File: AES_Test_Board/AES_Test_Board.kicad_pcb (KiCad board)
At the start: 2 copper layers, 60 x 65 mm, 36 parts, among them J1 Conn_02x06_Top_Bottom, J2 Conn_02x06_Top_Bottom, U3 TCR3RM10A

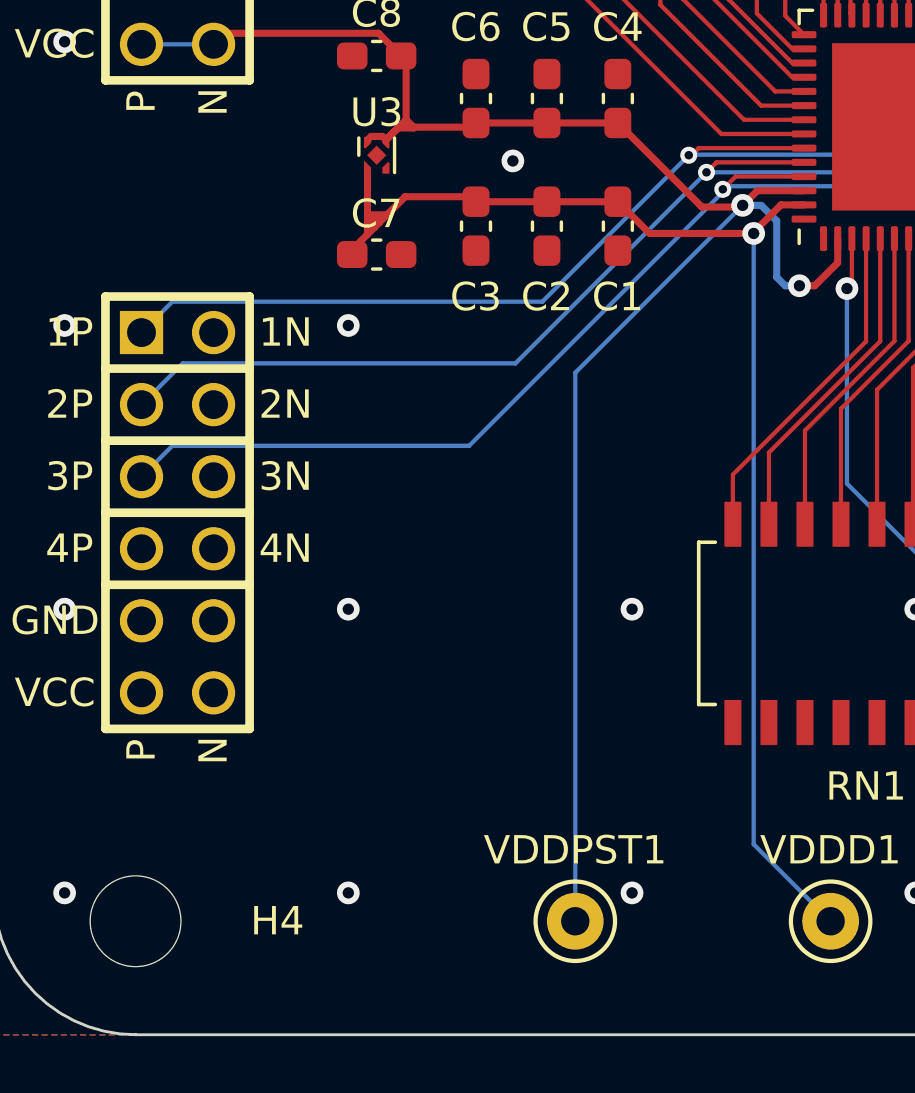
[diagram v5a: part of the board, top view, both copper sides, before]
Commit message: Created Bitstreams for both FPGA's
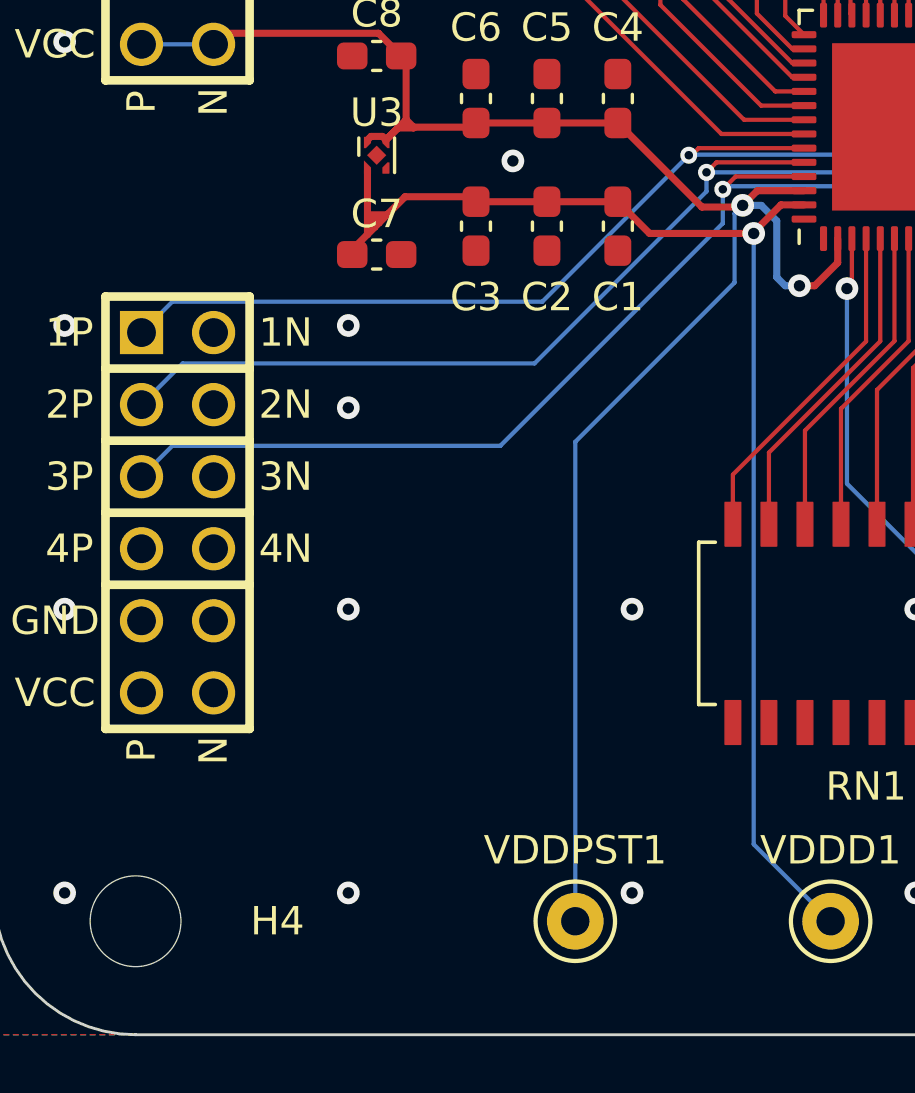
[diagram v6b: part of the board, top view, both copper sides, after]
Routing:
- net /VSS: vias 31 -> 32
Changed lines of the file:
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@@
   (via (at 113.2 90.2) (size 0.6) (drill 0.3) (layers "F.Cu" "B.Cu") (net 3))
   (segment (start 113.308738 90.091262) (end 129.091262 90.091262) (width 0.15) (layer "B.Cu") (net 3))
-  (segment (start 113.360202 90.360202) (end 113.2 90.2) (width 0.15) (layer "B.Cu") (net 3))
-  (segment (start 113.139798 90.360202) (end 113.360202 90.360202) (width 0.15) (layer "B.Cu") (net 3))
-  (segment (start 93.797 99.243) (end 104.257 99.243) (width 0.15) (layer "B.Cu") (net 3))
-  (segment (start 104.257 99.243) (end 113.139798 90.360202) (width 0.15) (layer "B.Cu") (net 3))
+  (segment (start 113.2 91.4) (end 113.2 90.2) (width 0.15) (layer "B.Cu") (net 3))
+  (segment (start 93.797 99.243) (end 105.357 99.243) (width 0.15) (layer "B.Cu") (net 3))
+  (segment (start 92.71 100.33) (end 93.797 99.243) (width 0.15) (layer "B.Cu") (net 3))
   (segment (start 113.2 90.2) (end 113.308738 90.091262) (width 0.15) (layer "B.Cu") (net 3))
-  (segment (start 92.71 100.33) (end 93.797 99.243) (width 0.15) (layer "B.Cu") (net 3))
+  (segment (start 105.357 99.243) (end 113.2 91.4) (width 0.15) (layer "B.Cu") (net 3))
   (segment (start 129.091262 90.091262) (end 144.5 105.5) (width 0.15) (layer "B.Cu") (net 3))
   (segment (start 112.977462 89.25) (end 116.0625 89.25) (width 0.15) (layer "F.Cu") (net 4))
   (segment (start 112.624876 89.602586) (end 112.977462 89.25) (width 0.15) (layer "F.Cu") (net 4))
   (via (at 112.624876 89.602586) (size 0.6) (drill 0.3) (layers "F.Cu" "B.Cu") (net 4))
-  (segment (start 112.624876 89.602586) (end 105.890462 96.337) (width 0.15) (layer "B.Cu") (net 4))
-  (segment (start 105.890462 96.337) (end 94.163 96.337) (width 0.15) (layer "B.Cu") (net 4))
+  (segment (start 106.563 96.337) (end 94.163 96.337) (width 0.15) (layer "B.Cu") (net 4))
   (segment (start 94.163 96.337) (end 92.71 97.79) (width 0.15) (layer "B.Cu") (net 4))
+  (segment (start 112.624876 89.602586) (end 112.624876 90.275124) (width 0.15) (layer "B.Cu") (net 4))
   (segment (start 136.102586 89.602586) (end 144.5 98) (width 0.15) (layer "B.Cu") (net 4))
+  (segment (start 112.624876 90.275124) (end 106.563 96.337) (width 0.15) (layer "B.Cu") (net 4))
   (segment (start 112.624876 89.602586) (end 136.102586 89.602586) (width 0.15) (layer "B.Cu") (net 4))
   (via (at 105.1 73) (size 0.6) (drill 0.3) (layers "F.Cu" "B.Cu") (free) (net 5))
@@
   (via (at 103.4 74.3) (size 0.6) (drill 0.3) (layers "F.Cu" "B.Cu") (free) (net 5))
   (via (at 103.4 79.9) (size 0.6) (drill 0.3) (layers "F.Cu" "B.Cu") (free) (net 5))
+  (via (at 100 97.9) (size 0.8) (drill 0.4) (layers "F.Cu" "B.Cu") (free) (net 5))
   (via (at 130 115) (size 0.8) (drill 0.4) (layers "F.Cu" "B.Cu") (free) (net 5))
   (via (at 103.4 81.7) (size 0.6) (drill 0.3) (layers "F.Cu" "B.Cu") (free) (net 5))
@@
   (via (at 115.9 93.6) (size 0.8) (drill 0.4) (layers "F.Cu" "B.Cu") (net 22))
   (via (at 113.898894 90.766262) (size 0.8) (drill 0.4) (layers "F.Cu" "B.Cu") (net 22))
+  (segment (start 108 99.1) (end 113.613198 93.486802) (width 0.15) (layer "B.Cu") (net 22))
   (segment (start 114.554765 90.766262) (end 115.1 91.311497) (width 0.25) (layer "B.Cu") (net 22))
+  (segment (start 113.613198 91.051958) (end 113.898894 90.766262) (width 0.15) (layer "B.Cu") (net 22))
   (segment (start 115.1 93.3) (end 115.4 93.6) (width 0.25) (layer "B.Cu") (net 22))
-  (segment (start 108 96.665156) (end 113.898894 90.766262) (width 0.15) (layer "B.Cu") (net 22))
   (segment (start 115.4 93.6) (end 115.9 93.6) (width 0.25) (layer "B.Cu") (net 22))
   (segment (start 115.1 91.311497) (end 115.1 93.3) (width 0.25) (layer "B.Cu") (net 22))
   (segment (start 92.71 85.09) (end 95.25 85.09) (width 0.15) (layer "B.Cu") (net 22))
-  (segment (start 108 116) (end 108 96.665156) (width 0.15) (layer "B.Cu") (net 22))
+  (segment (start 108 116) (end 108 99.1) (width 0.15) (layer "B.Cu") (net 22))
   (segment (start 113.898894 90.766262) (end 114.554765 90.766262) (width 0.25) (layer "B.Cu") (net 22))
+  (segment (start 113.613198 93.486802) (end 113.613198 91.051958) (width 0.15) (layer "B.Cu") (net 22))
   (segment (start 101.08125 91.38125) (end 101 91.3) (width 0.25) (layer "F.Cu") (net 24))
   (segment (start 101.3625 91.1) (end 101.38125 91.08125) (width 0.25) (layer "F.Cu") (net 24))

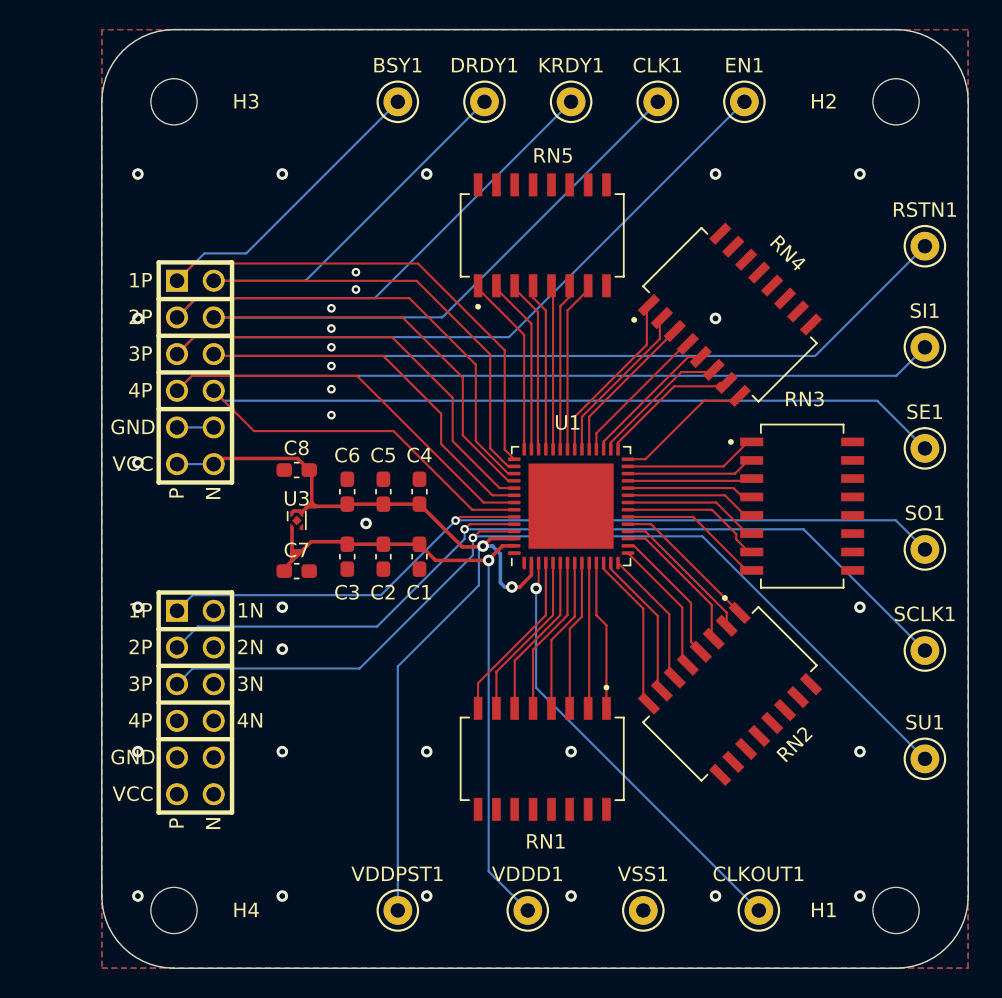
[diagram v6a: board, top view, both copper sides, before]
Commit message: Added Power measurement circuitry and regenerated gerbers
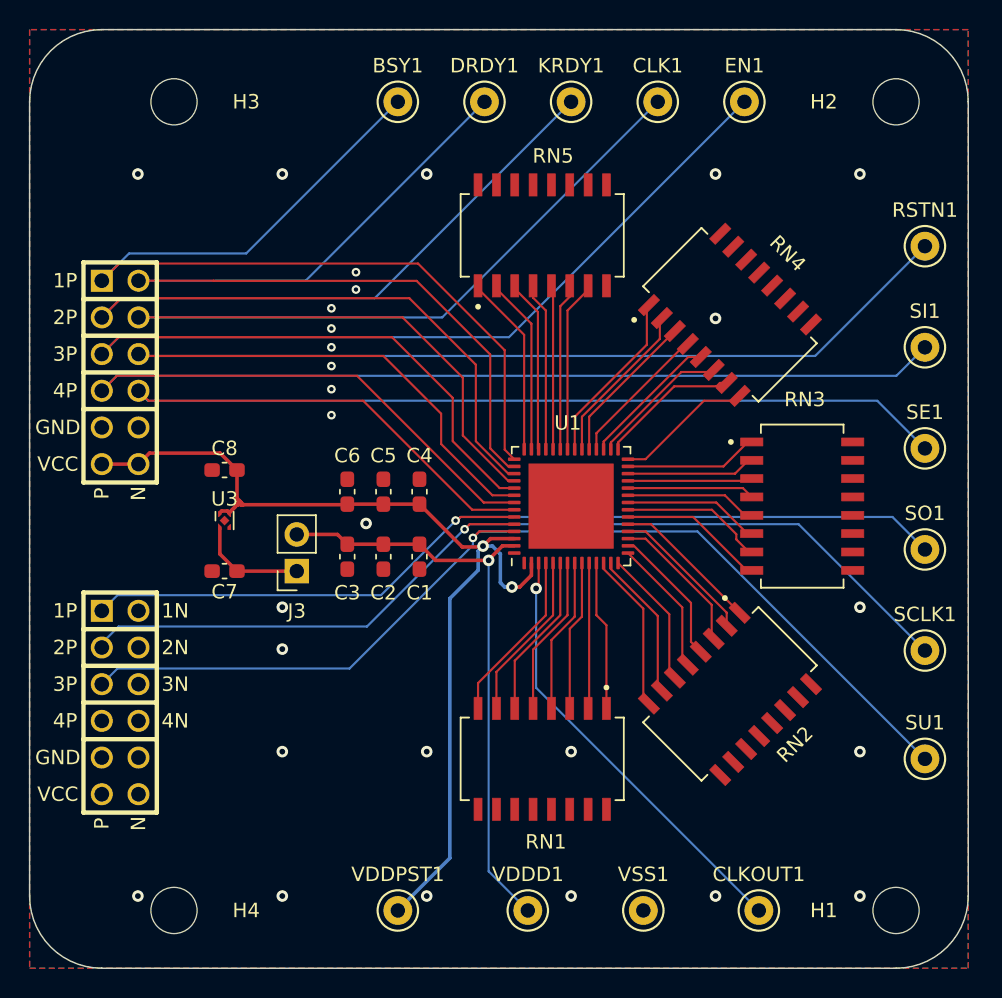
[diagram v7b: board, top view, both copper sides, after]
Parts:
- added J3: Conn_01x02_Pin, Connector_PinSocket_2.54mm:PinSocket_1x02_P2.54mm_Vertical, F.Cu at (101.0, 92.5)
- moved J1 5.21 mm to (88.8, 78.7)
- moved J2 5.21 mm to (88.8, 101.6)
- moved C7 5.00 mm to (96.0, 92.5), turned to 180 degrees
- moved C8 5.00 mm to (96.0, 85.5)
- moved U3 5.00 mm to (96.0, 89.0)
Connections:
- C7 pad 1: /VDDD -> Net-(J3-Pin_1)
- U3 pad 1: /VDDD -> Net-(J3-Pin_1)
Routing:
- net /SCAN_ENABLE: track 75.1 -> 85.6 mm
- net /BSY: track 53.9 -> 64.3 mm
- net /KRDY: track 65.5 -> 75.9 mm
- net /SCAN_IN: track 80.5 -> 90.9 mm
- net /RSTN: track 78.5 -> 89.0 mm
- net /ENABLE: track 76.4 -> 86.9 mm
- net /DRDY: track 53.8 -> 64.3 mm
- net /CLK: track 64.8 -> 75.2 mm
- net Net-(J3-Pin_1): track 0.00 -> 7.59 mm
- net /VDDPST: track 65.3 -> 71.5 mm
- net /VDDD: track 47.1 -> 41.6 mm
- net /SCAN_OUT: track 59.2 -> 64.6 mm
- net /SCAN_UPDATE: track 66.2 -> 71.2 mm
- net /SCAN_CLK: track 62.6 -> 67.6 mm
- net /VSS: track 2.54 -> 0.00 mm, vias 32 -> 28
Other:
- board size 60 x 65 mm -> 65 x 65 mm

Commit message: Fixed board to match pinout
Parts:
- added G***: LOGO, Connector:GroupNegative, B.Cu at (119.5, 80.2)
- moved BSY1 59.0 mm to (145.0, 106.0)
- moved SU1 47.2 mm to (132.0, 60.0)
- moved SCLK1 45.2 mm to (120.0, 60.0)
- moved DRDY1 43.8 mm to (145.0, 91.0)
- moved SI1 40.3 mm to (108.0, 60.0)
- moved KRDY1 34.7 mm to (145.0, 84.0)
- moved SE1 30.3 mm to (126.0, 60.0)
- moved EN1 16.4 mm to (145.0, 70.0)
- moved CLK1 12.0 mm to (114.0, 60.0)
- moved RSTN1 7.02 mm to (145.0, 77.0)
- moved SO1 7.02 mm to (145.0, 98.0)
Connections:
- J1 pad 1: /BSY -> /SCAN_IN
- J1 pad 10: /SCAN_ENABLE -> /KRDY
- J1 pad 2: /KRDY -> /SCAN_CLK
- J1 pad 3: /ENABLE -> /SCAN_UPDATE
- J1 pad 4: /SCAN_IN -> /RSTN
- J1 pad 7: /DRDY -> /CLK
- J1 pad 8: /CLK -> /SCAN_ENABLE
- J1 pad 9: /RSTN -> /ENABLE
- J2 pad 1: /SCAN_OUT -> /DRDY
- J2 pad 2: /SCAN_CLK -> /SCAN_OUT
- J2 pad 3: /SCAN_UPDATE -> /BSY
- RN1 pad 7: /MLPIN5 -> unconnected-(RN1-Pad7)
- RN1 pad 8: /MLPIN4 -> unconnected-(RN1-Pad8)
- RN2 pad 1: /MLPIN19 -> unconnected-(RN2-Pad1)
- RN3 pad 2: /MLPIN26 -> unconnected-(RN3-Pad2)
- U1 pad 1: /VSS -> /CLKOUT
- U1 pad 19: /MLPIN19 -> unconnected-(U1-MLPINS-Pad19)
- U1 pad 2: /VDDPST -> /SCAN_OUT
- U1 pad 26: /MLPIN26 -> unconnected-(U1-MLPINS-Pad26)
- U1 pad 3: /CLKOUT -> /BSY
- U1 pad 4: /MLPIN4 -> unconnected-(U1-MLPINS-Pad4)
- U1 pad 43: /BSY -> /SCAN_IN
- U1 pad 44: /DRDY -> /CLK
- U1 pad 45: /KRDY -> /SCAN_CLK
- U1 pad 46: /CLK -> /SCAN_ENABLE
- U1 pad 47: /ENABLE -> /SCAN_UPDATE
- U1 pad 48: /RSTN -> /ENABLE
- U1 pad 49: /SCAN_IN -> /RSTN
- U1 pad 5: /MLPIN5 -> unconnected-(U1-MLPINS-Pad5)
- U1 pad 50: /SCAN_ENABLE -> /KRDY
- U1 pad 51: /SCAN_OUT -> /DRDY
- U1 pad 52: /SCAN_CLK -> /VSS
- U1 pad 53: /SCAN_UPDATE -> /VSS
- U1 pad 54: /VDDPST -> /VDDD
- U1 pad 55: /VDDD -> /VDDPST
- U1 pad 56: /VSS -> /VDDPST
- U1 pad 57: (no net) -> /VSS
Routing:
- net /SCAN_IN: track 90.9 -> 64.3 mm
- net /SCAN_UPDATE: track 71.2 -> 86.9 mm, vias 1 -> 0
- net /MLPIN4: track 12.0 -> 0.00 mm
- net /MLPIN5: track 11.7 -> 0.00 mm
- net /CLK: track 75.2 -> 64.3 mm
- net /SCAN_ENABLE: track 85.6 -> 75.2 mm
- net /MLPIN19: track 10.3 -> 0.00 mm
- net /KRDY: track 75.9 -> 85.6 mm
- net /MLPIN26: track 8.96 -> 0.00 mm
- net /SCAN_CLK: track 67.6 -> 75.9 mm, vias 1 -> 0
- net /VDDPST: track 71.5 -> 63.8 mm, vias 2 -> 1
- net /VSS: track 0.00 -> 4.29 mm, vias 28 -> 38
- net /BSY: track 64.3 -> 68.0 mm, vias 0 -> 1
- net /CLKOUT: track 30.5 -> 33.3 mm
- net /ENABLE: track 86.9 -> 89.0 mm
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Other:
- board text added: "Manthan Upadhyaya Linshen Liu Mohit Indumukhi Jaspreet Pawa Nishant Gupta"
